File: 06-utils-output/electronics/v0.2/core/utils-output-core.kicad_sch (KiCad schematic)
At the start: 8 parts, among them J1 Conn_02x06_Odd_Even, J4 Conn_02x04_Odd_Even, J5 Conn_02x02_Odd_Even, J6 Conn_02x05_Odd_Even

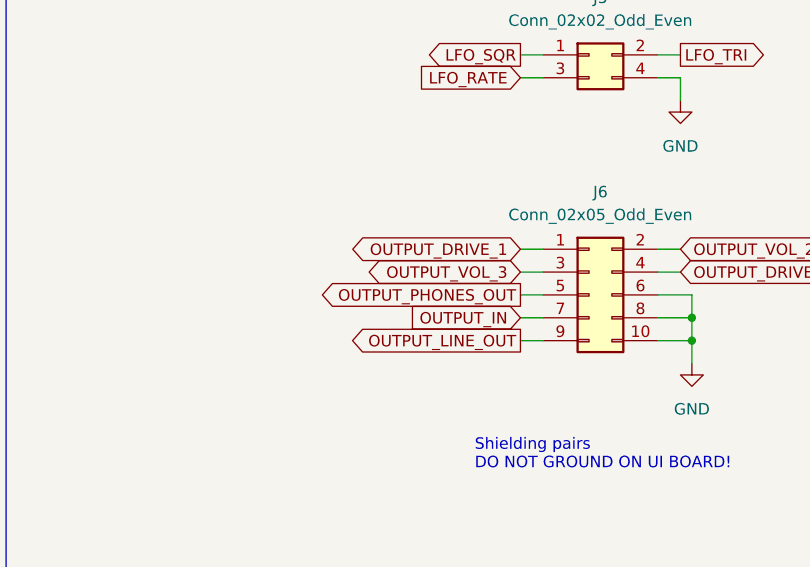
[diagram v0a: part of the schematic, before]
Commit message: Rearranged Utils+Output core PCB
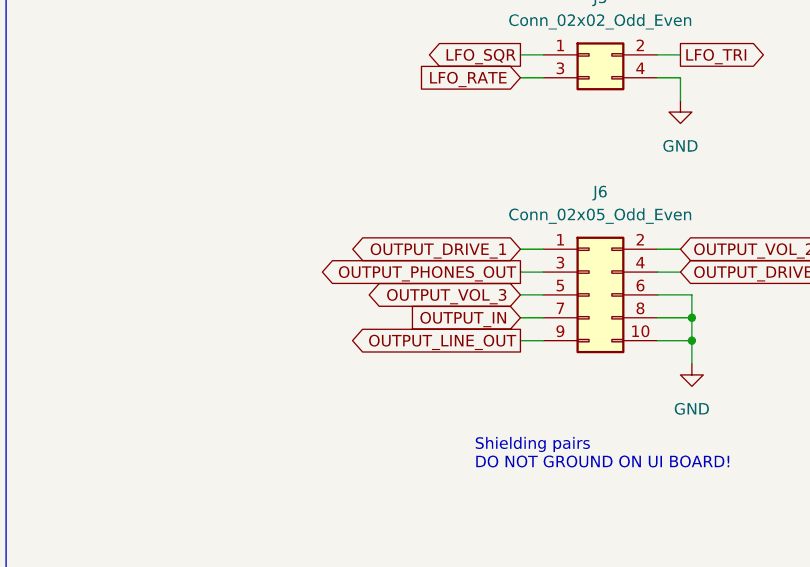
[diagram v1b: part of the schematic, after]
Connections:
- net OUTPUT_PHONES_OUT: now also J6.3 (Pin_3); no longer J6.5 (Pin_5)
- net OUTPUT_VOL_3: now also J6.5 (Pin_5); no longer J6.3 (Pin_3)
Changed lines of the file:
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@@
 	(global_label "OUTPUT_PHONES_OUT"
 		(shape output)
-		(at 208.28 121.92 180)
-		(fields_autoplaced yes)
-		(effects
-			(font
-				(size 1.27 1.27)
-			)
-			(justify right)
-		)
-		(property "Intersheetrefs" "${INTERSHEET_REFS}"
-			(at 184.9143 121.92 0)
+		(at 208.28 119.38 180)
+		(fields_autoplaced yes)
+		(effects
+			(font
+				(size 1.27 1.27)
+			)
+			(justify right)
+		)
+		(property "Intersheetrefs" "${INTERSHEET_REFS}"
+			(at 184.9143 119.38 0)
 			(effects
 				(font
@@
 	(global_label "OUTPUT_VOL_3"
 		(shape bidirectional)
-		(at 208.28 119.38 180)
-		(fields_autoplaced yes)
-		(effects
-			(font
-				(size 1.27 1.27)
-			)
-			(justify right)
-		)
-		(property "Intersheetrefs" "${INTERSHEET_REFS}"
-			(at 190.3949 119.38 0)
-			(effects
-				(font
+		(at 208.28 121.92 180)
+		(fields_autoplaced yes)
+		(effects
+			(font
+				(size 1.27 1.27)
+			)
+			(justify right)
+		)
+		(property "Intersheetrefs" "${INTERSHEET_REFS}"
+			(at 190.3949 121.92 0)
+			(effects
+				(font

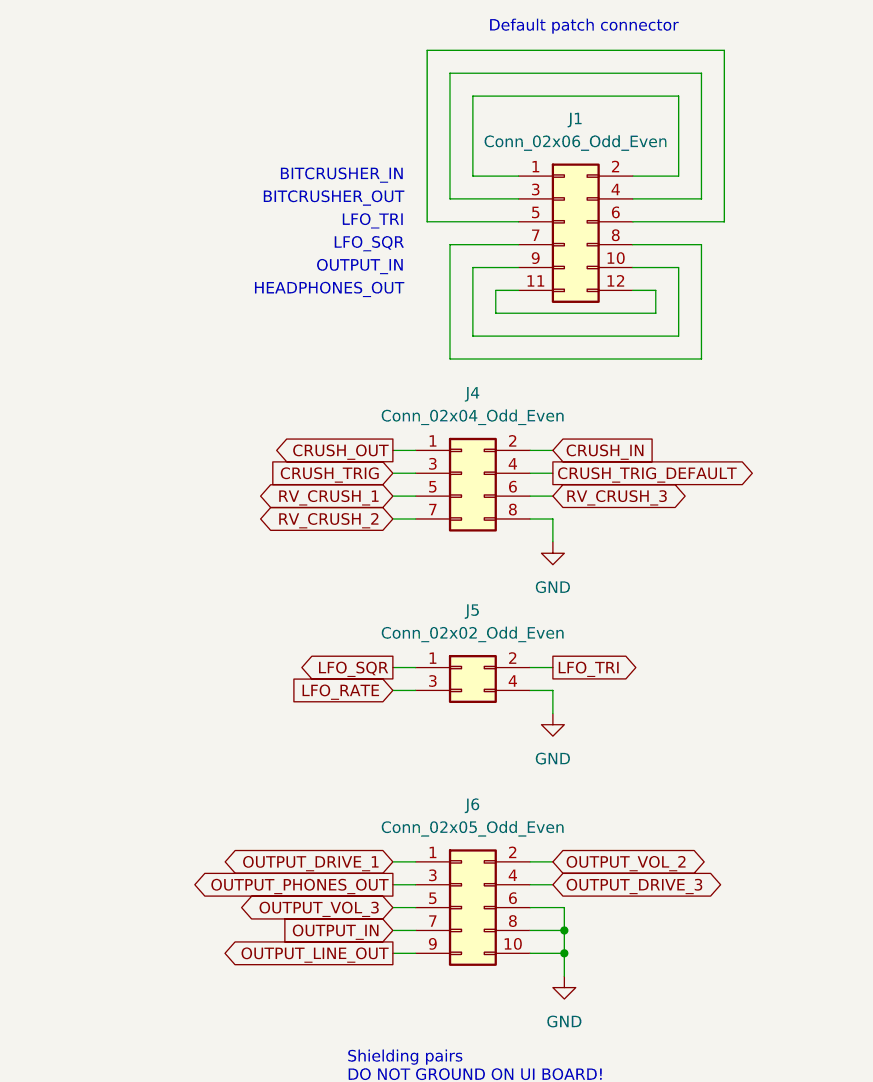
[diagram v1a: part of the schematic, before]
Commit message: Redesigned output module
- The master volume was _before_ the gain control which made no sense because the volume had an effect on how much signal went into the gain stage. Now the master volume is after the diode limiter/clamper which means the output can be tamed while keeping the overdrive.
- Rearranged the output resistors so now line out has a 1k resistor.
- STILL TODO: the headphone output is not protected against accidental +/-12V inputs.
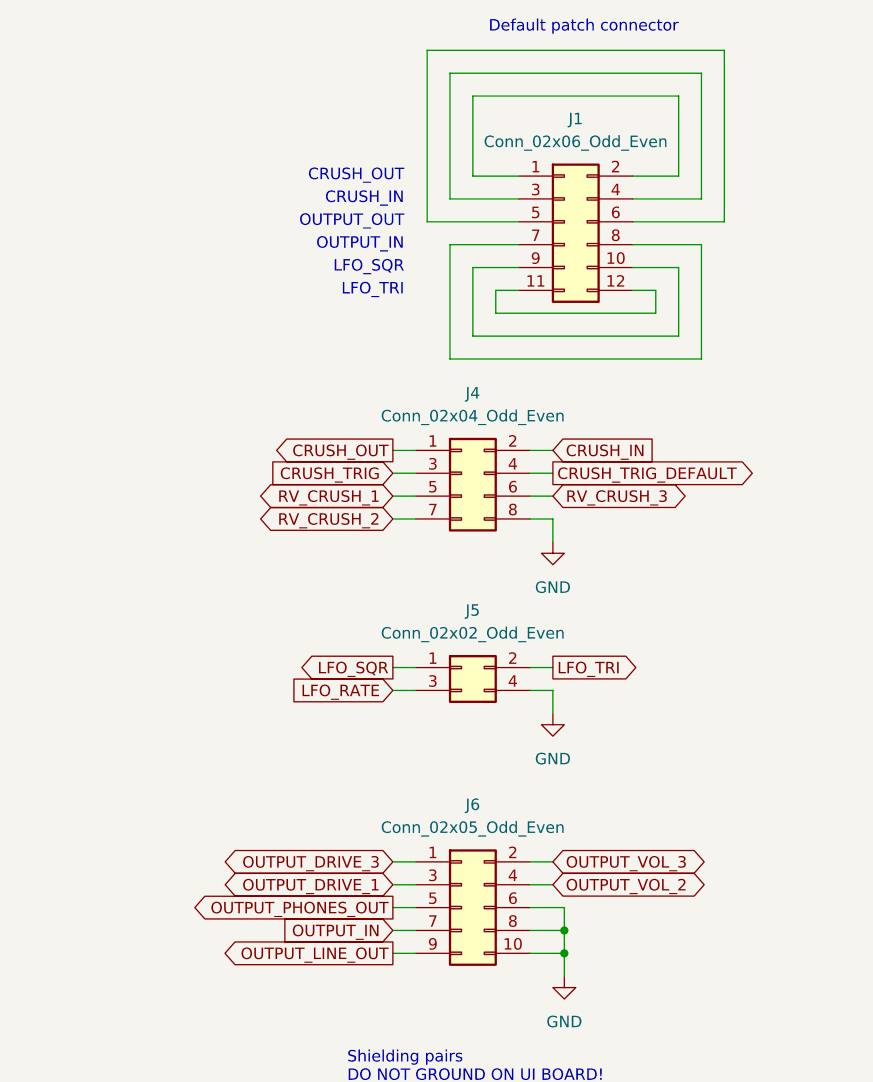
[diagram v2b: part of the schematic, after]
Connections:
- net OUTPUT_DRIVE_1: now also J6.3 (Pin_3); no longer J6.1 (Pin_1)
- net OUTPUT_DRIVE_3: now also J6.1 (Pin_1); no longer J6.4 (Pin_4)
- net OUTPUT_PHONES_OUT: now also J6.5 (Pin_5); no longer J6.3 (Pin_3)
- net OUTPUT_VOL_2: now also J6.4 (Pin_4); no longer J6.2 (Pin_2)
- net OUTPUT_VOL_3: now also J6.2 (Pin_2); no longer J6.5 (Pin_5)
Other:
- note added: "CRUSH_IN"
- note added: "CRUSH_OUT"
- note added: "OUTPUT_OUT"
- note removed: "BITCRUSHER_IN"
- note removed: "BITCRUSHER_OUT"
- note removed: "HEADPHONES_OUT"
